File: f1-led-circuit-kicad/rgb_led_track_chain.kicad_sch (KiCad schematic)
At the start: 30 parts, among them U34 HD108-2020, U35 HD108-2020, U36 HD108-2020, U37 HD108-2020, U38 HD108-2020, U39 HD108-2020, U40 HD108-2020, U41 HD108-2020, U42 HD108-2020, U43 HD108-2020, U44 HD108-2020, U45 HD108-2020, U46 HD108-2020, U47 HD108-2020, U48 HD108-2020, U49 HD108-2020, U50 HD108-2020, U51 HD108-2020, U52 HD108-2020, U53 HD108-2020, U54 HD108-2020, U55 HD108-2020, U56 HD108-2020, U57 HD108-2020, U58 HD108-2020, U59 HD108-2020, U60 HD108-2020, U61 HD108-2020, U62 HD108-2020, U63 HD108-2020

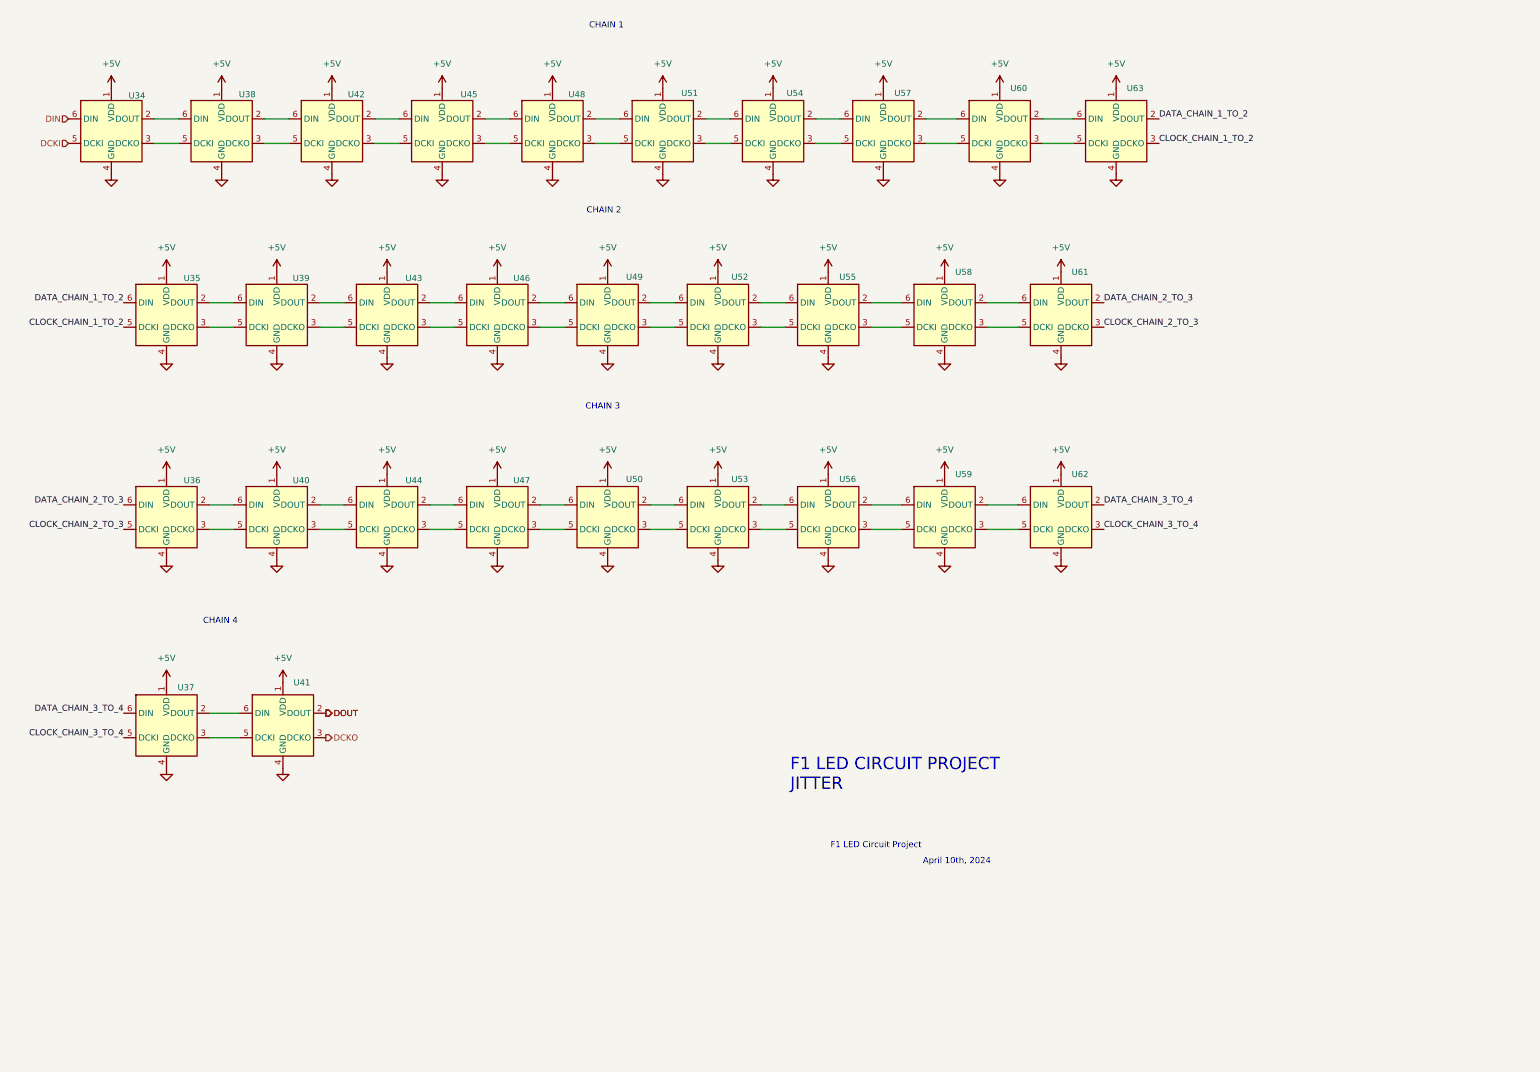
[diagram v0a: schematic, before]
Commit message: KiCad - Fix pull-up resistors, ground jumper, clean labels, add decoupling capacitor DNI footprints to LEDs
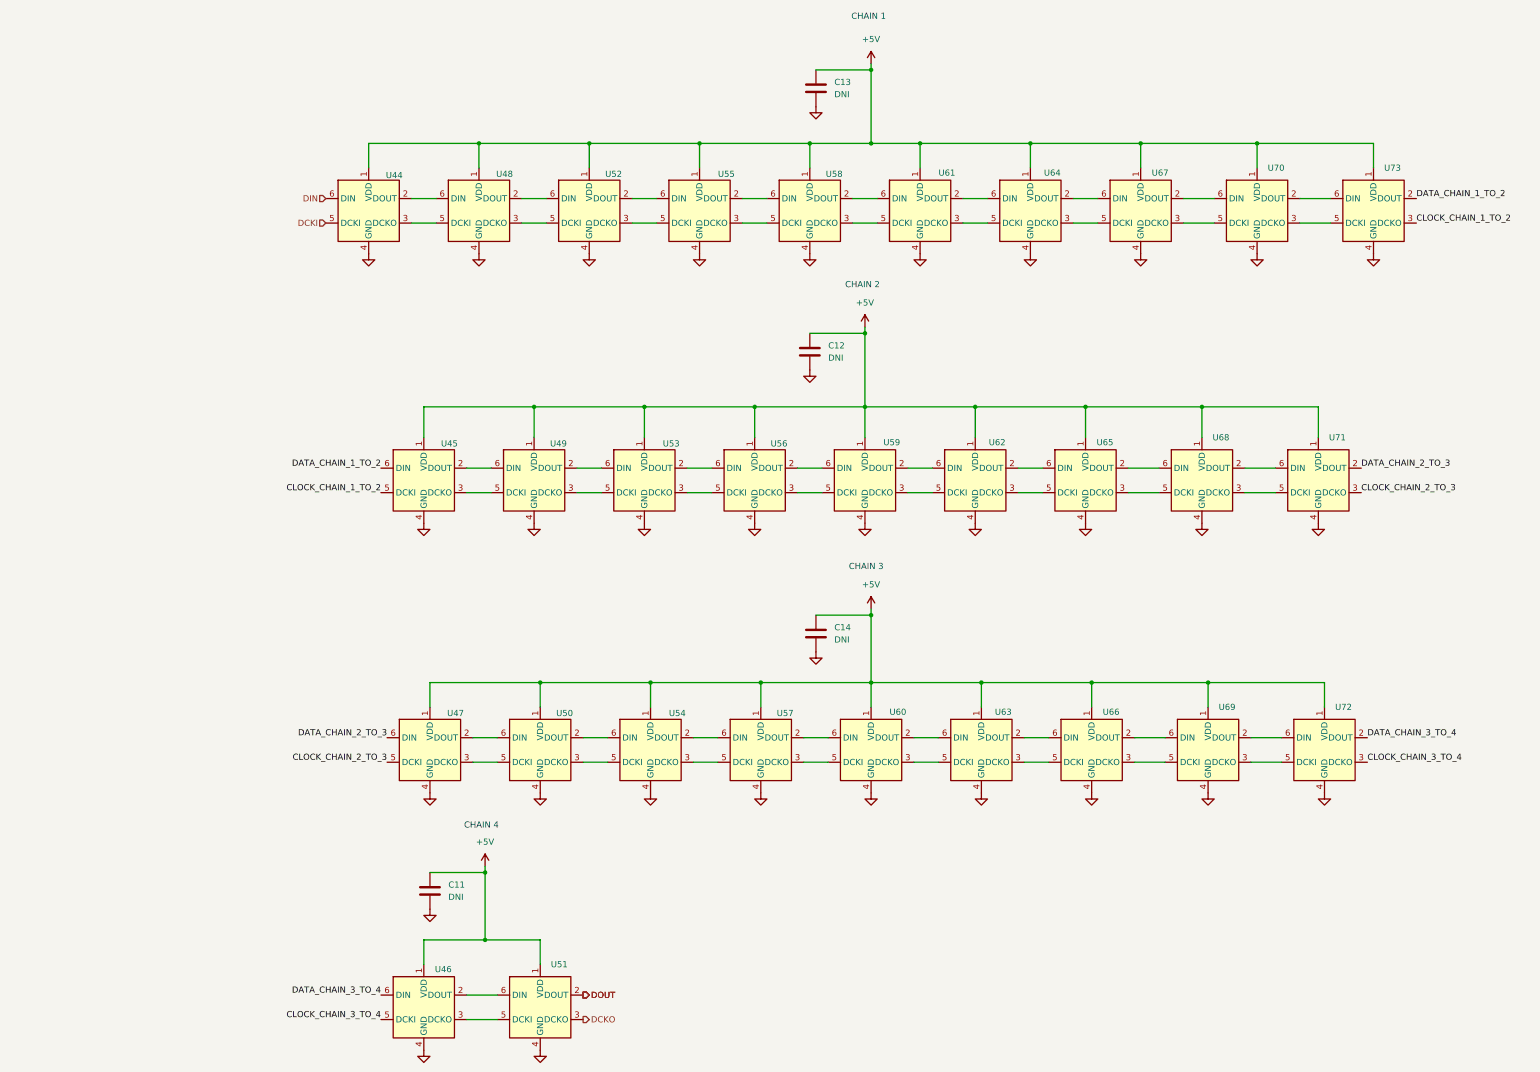
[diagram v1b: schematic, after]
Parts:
- added C11, C12, C13, C14: DNI, Capacitor_SMD:C_0805_2012Metric, symbol Device:C
- renumbered U34 to U44, U35 to U45, U37 to U46, U36 to U47, U38 to U48, U39 to U49, U40 to U50, U41 to U51, U42 to U52, U43 to U53, U44 to U54, U45 to U55, U46 to U56, U47 to U57, U48 to U58, U49 to U59, U50 to U60, U51 to U61, U52 to U62, U53 to U63, U54 to U64, U55 to U65, U56 to U66, U57 to U67, U58 to U68, U59 to U69, U60 to U70, U61 to U71, U62 to U72, U63 to U73
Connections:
- net +5V: now also C11.1, C12.1, C13.1, C14.1
- net GND: now also C11.2, C12.2, C13.2, C14.2
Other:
- note removed: "April 10th, 2024"
- note removed: "F1 LED CIRCUIT PROJECT JITTER"
- note removed: "F1 LED Circuit Project"
- company: (none) -> JITTER
- title: (none) -> F1 LED CIRCUIT PROJECT
- moved on the sheet: U44, U45, U46, U47, U48, U49, U50, U51, U52, U53, U54, U55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

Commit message: KiCad - Update reference numbers for LEDs
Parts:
- renumbered U55 to U10, U58 to U11, U61 to U12, U64 to U13, U67 to U14, U70 to U15, U73 to U16, U45 to U17, U49 to U18, U53 to U19, U56 to U20, U59 to U21, U62 to U22, U65 to U23, U68 to U24, U71 to U25, U47 to U26, U50 to U27, U54 to U28, U57 to U29, U60 to U30, U63 to U31, U66 to U32, U69 to U33, U72 to U34, U46 to U35, U51 to U36, U44 to U7, U48 to U8, U52 to U9

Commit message: KiCad - Update schematic - LED Pins Fix
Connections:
- net CLOCK_CHAIN_1_TO_2: now also U16.2 (DCKO); no longer U16.3 (DCKO)
- net CLOCK_CHAIN_2_TO_3: now also U25.2 (DCKO); no longer U25.3 (DCKO)
- net CLOCK_CHAIN_3_TO_4: now also U34.2 (DCKO); no longer U34.3 (DCKO)
- net DATA_CHAIN_1_TO_2: now also U16.3 (DOUT); no longer U16.2 (DOUT)
- net DATA_CHAIN_2_TO_3: now also U25.3 (DOUT); no longer U25.2 (DOUT)
- net DATA_CHAIN_3_TO_4: now also U34.3 (DOUT); no longer U34.2 (DOUT)
- net DCKO: now also U36.2 (DCKO); no longer U36.3 (DCKO)
- net DOUT: now also U36.3 (DOUT); no longer U36.2 (DOUT)
- net at U34.5 (DCKI): now also U33.2 (DCKO); no longer U33.3 (DCKO)
- net at U34.6 (DIN): now also U33.3 (DOUT); no longer U33.2 (DOUT)
- net at U36.5 (DCKI): now also U35.2 (DCKO); no longer U35.3 (DCKO)
- net at U36.6 (DIN): now also U35.3 (DOUT); no longer U35.2 (DOUT)
- net at U17.2 (DCKO): now also U18.5 (DCKI); no longer U18.6 (DIN)
- net at U17.3 (DOUT): now also U18.6 (DIN); no longer U18.5 (DCKI)
- net at U31.2 (DCKO): now also U32.5 (DCKI); no longer U32.6 (DIN)
- net at U31.3 (DOUT): now also U32.6 (DIN); no longer U32.5 (DCKI)
- net at U31.5 (DCKI): now also U30.2 (DCKO); no longer U30.3 (DCKO)
- net at U31.6 (DIN): now also U30.3 (DOUT); no longer U30.2 (DOUT)
- net at U32.2 (DCKO): now also U33.5 (DCKI); no longer U33.6 (DIN)
- net at U32.3 (DOUT): now also U33.6 (DIN); no longer U33.5 (DCKI)
- net at U11.2 (DCKO): now also U12.5 (DCKI); no longer U12.6 (DIN)
- net at U11.3 (DOUT): now also U12.6 (DIN); no longer U12.5 (DCKI)
- net at U11.5 (DCKI): now also U10.2 (DCKO); no longer U10.3 (DCKO)
- net at U11.6 (DIN): now also U10.3 (DOUT); no longer U10.2 (DOUT)
- net at U22.2 (DCKO): now also U23.5 (DCKI); no longer U23.6 (DIN)
- net at U22.3 (DOUT): now also U23.6 (DIN); no longer U23.5 (DCKI)
- net at U22.5 (DCKI): now also U21.2 (DCKO); no longer U21.3 (DCKO)
- net at U22.6 (DIN): now also U21.3 (DOUT); no longer U21.2 (DOUT)
- net at U25.5 (DCKI): now also U24.2 (DCKO); no longer U24.3 (DCKO)
- net at U25.6 (DIN): now also U24.3 (DOUT); no longer U24.2 (DOUT)
- net at U8.2 (DCKO): now also U9.5 (DCKI); no longer U9.6 (DIN)
- net at U8.3 (DOUT): now also U9.6 (DIN); no longer U9.5 (DCKI)
- net at U8.5 (DCKI): now also U7.2 (DCKO); no longer U7.3 (DCKO)
- net at U8.6 (DIN): now also U7.3 (DOUT); no longer U7.2 (DOUT)
- net at U27.2 (DCKO): now also U28.5 (DCKI); no longer U28.6 (DIN)
- net at U27.3 (DOUT): now also U28.6 (DIN); no longer U28.5 (DCKI)
- net at U27.5 (DCKI): now also U26.2 (DCKO); no longer U26.3 (DCKO)
- net at U27.6 (DIN): now also U26.3 (DOUT); no longer U26.2 (DOUT)
- net at U30.5 (DCKI): now also U29.2 (DCKO); no longer U29.3 (DCKO)
- net at U30.6 (DIN): now also U29.3 (DOUT); no longer U29.2 (DOUT)
- net at U20.2 (DCKO): now also U21.5 (DCKI); no longer U21.6 (DIN)
- net at U20.3 (DOUT): now also U21.6 (DIN); no longer U21.5 (DCKI)
- net at U20.5 (DCKI): now also U19.2 (DCKO); no longer U19.3 (DCKO)
- net at U20.6 (DIN): now also U19.3 (DOUT); no longer U19.2 (DOUT)
- net at U24.5 (DCKI): now also U23.2 (DCKO); no longer U23.3 (DCKO)
- net at U24.6 (DIN): now also U23.3 (DOUT); no longer U23.2 (DOUT)
- net at U16.5 (DCKI): now also U15.2 (DCKO); no longer U15.3 (DCKO)
- net at U16.6 (DIN): now also U15.3 (DOUT); no longer U15.2 (DOUT)
- net at U9.2 (DCKO): now also U10.5 (DCKI); no longer U10.6 (DIN)
- net at U9.3 (DOUT): now also U10.6 (DIN); no longer U10.5 (DCKI)
- net at U14.2 (DCKO): now also U15.5 (DCKI); no longer U15.6 (DIN)
- net at U14.3 (DOUT): now also U15.6 (DIN); no longer U15.5 (DCKI)
- net at U14.5 (DCKI): now also U13.2 (DCKO); no longer U13.3 (DCKO)
- net at U14.6 (DIN): now also U13.3 (DOUT); no longer U13.2 (DOUT)
- net at U13.5 (DCKI): now also U12.2 (DCKO); no longer U12.3 (DCKO)
- net at U13.6 (DIN): now also U12.3 (DOUT); no longer U12.2 (DOUT)
- net at U28.2 (DCKO): now also U29.5 (DCKI); no longer U29.6 (DIN)
- net at U28.3 (DOUT): now also U29.6 (DIN); no longer U29.5 (DCKI)
- net at U18.2 (DCKO): now also U19.5 (DCKI); no longer U19.6 (DIN)
- net at U18.3 (DOUT): now also U19.6 (DIN); no longer U19.5 (DCKI)

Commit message: KiCad - Update data sheet and part number for USB-C in schematic
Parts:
- renumbered C11 to C15, C12 to C16, C13 to C17, C14 to C18
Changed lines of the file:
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@@
 		(dnp no)
 		(fields_autoplaced yes)
-		(property "Reference" "C14"
+		(property "Reference" "C18"
 			(at 189.23 144.7799 0)
 			(effects
@@
 		(dnp no)
 		(fields_autoplaced yes)
-		(property "Reference" "#PWR063"
+		(property "Reference" "#PWR0101"
 			(at 195.58 86.36 0)
 			(effects
@@
 		(dnp no)
 		(fields_autoplaced yes)
-		(property "Reference" "#PWR062"
+		(property "Reference" "#PWR0100"
 			(at 185.42 156.21 0)
 			(effects
@@
 		(dnp no)
 		(fields_autoplaced yes)
-		(property "Reference" "#PWR061"
+		(property "Reference" "#PWR099"
 			(at 185.42 43.18 0)
 			(effects
@@
 		(dnp no)
 		(fields_autoplaced yes)
-		(property "Reference" "C11"
+		(property "Reference" "C15"
 			(at 109.22 198.1199 0)
 			(effects
@@
 		(dnp no)
 		(fields_autoplaced yes)
-		(property "Reference" "C12"
+		(property "Reference" "C16"
 			(at 187.96 86.3599 0)
 			(effects
@@
 		(dnp no)
 		(fields_autoplaced yes)
-		(property "Reference" "#PWR047"
+		(property "Reference" "#PWR085"
 			(at 105.41 209.55 0)
 			(effects
@@
 		(dnp no)
 		(fields_autoplaced yes)
-		(property "Reference" "#PWR065"
+		(property "Reference" "#PWR0103"
 			(at 196.85 31.75 0)
 			(effects
@@
 		(dnp no)
 		(fields_autoplaced yes)
-		(property "Reference" "C13"
+		(property "Reference" "C17"
 			(at 189.23 31.7499 0)
 			(effects
@@
 		(dnp no)
 		(fields_autoplaced yes)
-		(property "Reference" "#PWR066"
+		(property "Reference" "#PWR0104"
 			(at 196.85 144.78 0)
 			(effects
@@
 		(dnp no)
 		(fields_autoplaced yes)
-		(property "Reference" "#PWR049"
+		(property "Reference" "#PWR087"
 			(at 116.84 198.12 0)
 			(effects
@@
 		(dnp no)
 		(fields_autoplaced yes)
-		(property "Reference" "#PWR060"
+		(property "Reference" "#PWR098"
 			(at 184.15 97.79 0)
 			(effects

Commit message: KiCad - Add MPN for leds in schematic
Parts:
- U10, U11, U12, U13, U14, U15, U16, U17, U18, U19, U20, U21, U22, U23, U24, U25, U26, U27, U28, U29, U30, U31, U32, U33, U34, U35, U36, U7, U8, U9: MPN (none) -> HD108-2020

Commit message: Cleanup schematics and redundant vias in PCB
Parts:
- C15, C16, C17, C18: now not fitted
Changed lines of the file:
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@@
 		(in_bom yes)
 		(on_board yes)
-		(dnp no)
+		(dnp yes)
 		(fields_autoplaced yes)
 		(property "Reference" "C18"
@@
 		(in_bom yes)
 		(on_board yes)
-		(dnp no)
+		(dnp yes)
 		(fields_autoplaced yes)
 		(property "Reference" "C15"
@@
 		(in_bom yes)
 		(on_board yes)
-		(dnp no)
+		(dnp yes)
 		(fields_autoplaced yes)
 		(property "Reference" "C16"
@@
 		(in_bom yes)
 		(on_board yes)
-		(dnp no)
+		(dnp yes)
 		(fields_autoplaced yes)
 		(property "Reference" "C17"
